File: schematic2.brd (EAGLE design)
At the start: 101.6 x 53.3 mm, 76 parts, among them IC6 DS3231/SO

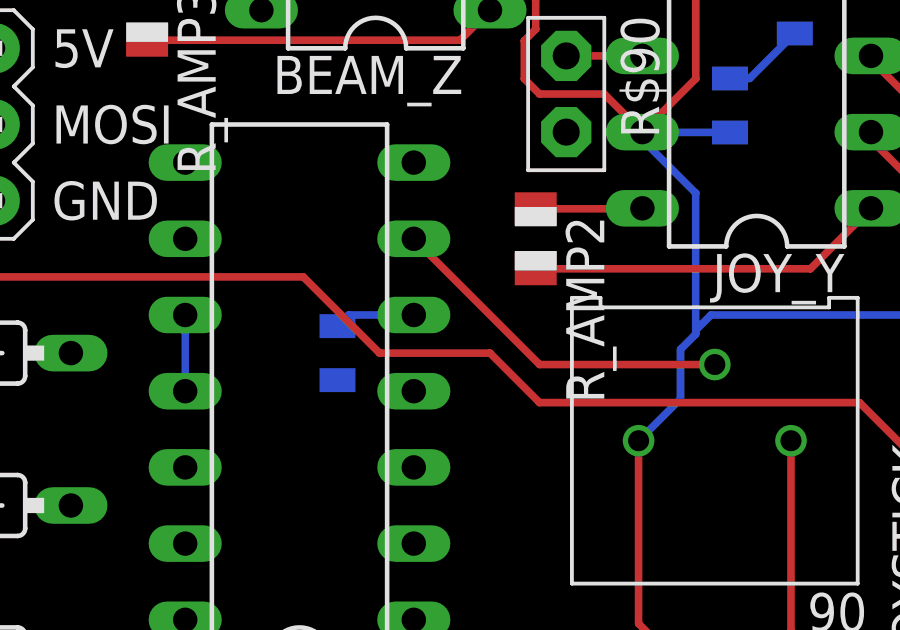
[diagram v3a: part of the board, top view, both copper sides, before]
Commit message: Corrected unity gain buffer amplifiers for reference voltages into the instrumentation amps.
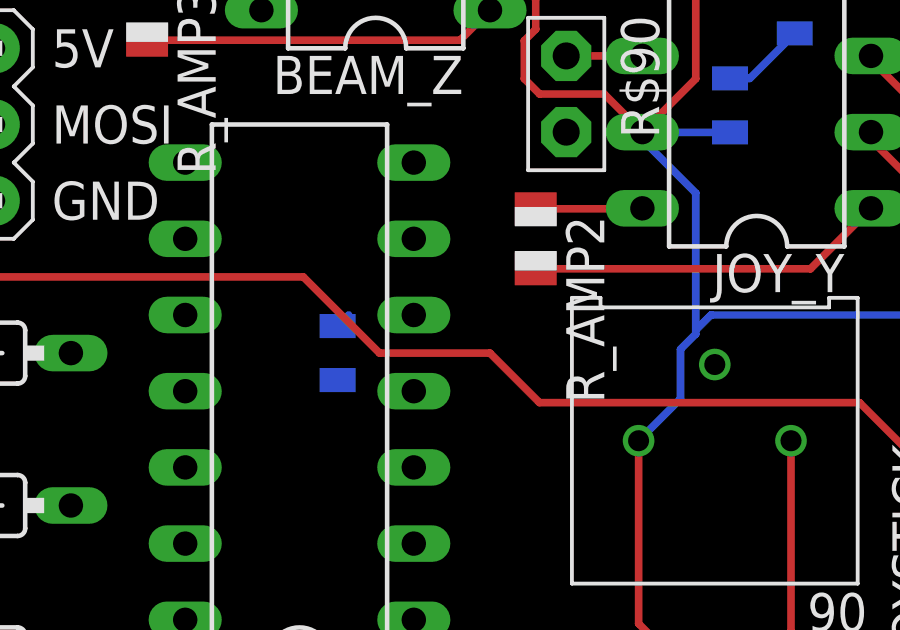
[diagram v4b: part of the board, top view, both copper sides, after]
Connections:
- new net REF_BEAM: BEAM_Z.5, REF.8, REF.9
- new net REF_JOYX: JOY_Y.5, REF.6, REF.7
- new net REF_JOYY: JOY_X.5, REF.1, REF.2
- net A3: now also REF.3; no longer JOY_X.5, REF.1, REF.2
- net A4: now also REF.5; no longer JOY_Y.5, REF.6, REF.7
- net A5: now also REF.10; no longer BEAM_Z.5, REF.8, REF.9
- net AGND: no longer REF.10, REF.3, REF.5
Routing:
- net A4: track 14.3 -> 2.54 mm
- net AGND: track 24.3 -> 19.6 mm
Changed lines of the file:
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@@
 <?xml version="1.0" encoding="utf-8"?>
 <!DOCTYPE eagle SYSTEM "eagle.dtd">
-<eagle version="7.2.0">
+<eagle version="7.0.0">
 <drawing>
 <settings>
@@
 <signals>
 <signal name="A4">
-<contactref element="REF" pad="6"/>
-<contactref element="JOY_Y" pad="5"/>
-<contactref element="REF" pad="7"/>
-<contactref element="90" pad="P$2-WIPER"/>
-<contactref element="4H" pad="A"/>
-<contactref element="4L" pad="C"/>
 <contactref element="U$1" pad="A4"/>
 <contactref element="ANALOG_IN" pad="4"/>
 <wire x1="60.96" y1="2.54" x2="60.96" y2="5.08" width="0.4064" layer="1"/>
-<wire x1="90.043" y1="19.939" x2="84.201" y2="19.939" width="0.254" layer="1"/>
-<wire x1="84.201" y1="19.939" x2="80.01" y2="24.13" width="0.254" layer="1"/>
-<wire x1="80.01" y1="26.67" x2="87.63" y2="32.766" width="0" layer="19" extent="1-1"/>
-<wire x1="80.01" y1="24.13" x2="80.01" y2="26.67" width="0" layer="19" extent="1-1"/>
-<wire x1="64.77" y1="12.7" x2="80.01" y2="24.13" width="0" layer="19" extent="1-1"/>
+<contactref element="4L" pad="C"/>
+<contactref element="90" pad="P$2-WIPER"/>
+<contactref element="4H" pad="A"/>
+<contactref element="REF" pad="5"/>
+<wire x1="80.01" y1="21.59" x2="90.043" y2="19.939" width="0" layer="19" extent="1-1"/>
+<wire x1="64.77" y1="12.7" x2="80.01" y2="21.59" width="0" layer="19" extent="1-1"/>
 <wire x1="60.96" y1="15.24" x2="64.77" y2="12.7" width="0" layer="19" extent="1-1"/>
 <wire x1="60.96" y1="5.08" x2="64.77" y2="12.7" width="0" layer="19" extent="1-1"/>
@@
 </signal>
 <signal name="A3">
-<contactref element="REF" pad="2"/>
-<contactref element="80" pad="P$2-WIPER"/>
-<contactref element="3H" pad="A"/>
-<contactref element="3L" pad="C"/>
-<contactref element="REF" pad="1"/>
-<contactref element="JOY_X" pad="5"/>
 <contactref element="U$1" pad="A3"/>
 <contactref element="ANALOG_IN" pad="5"/>
 <wire x1="58.42" y1="2.54" x2="58.42" y2="5.08" width="0.4064" layer="1"/>
-<wire x1="80.01" y1="13.97" x2="91.44" y2="43.053" width="0" layer="19" extent="1-1"/>
-<wire x1="80.01" y1="11.43" x2="80.01" y2="13.97" width="0" layer="19" extent="1-1"/>
-<wire x1="86.36" y1="9.652" x2="80.01" y2="11.43" width="0" layer="19" extent="1-1"/>
-<wire x1="64.77" y1="7.62" x2="80.01" y2="11.43" width="0" layer="19" extent="1-1"/>
+<contactref element="80" pad="P$2-WIPER"/>
+<contactref element="3L" pad="C"/>
+<contactref element="3H" pad="A"/>
+<contactref element="REF" pad="3"/>
+<wire x1="80.01" y1="16.51" x2="91.44" y2="43.053" width="0" layer="19" extent="1-1"/>
+<wire x1="64.77" y1="7.62" x2="80.01" y2="16.51" width="0" layer="19" extent="1-1"/>
 <wire x1="60.96" y1="10.16" x2="64.77" y2="7.62" width="0" layer="19" extent="1-1"/>
 <wire x1="58.42" y1="5.08" x2="60.96" y2="10.16" width="0" layer="19" extent="1-1"/>
@@
 </signal>
 <signal name="A5">
-<contactref element="BEAM_Z" pad="5"/>
-<contactref element="REF" pad="8"/>
-<contactref element="REF" pad="9"/>
-<contactref element="70" pad="P$2-WIPER"/>
-<contactref element="5H" pad="A"/>
-<contactref element="5L" pad="C"/>
 <contactref element="U$1" pad="A5"/>
 <contactref element="ANALOG_IN" pad="3"/>
 <wire x1="63.5" y1="2.54" x2="63.5" y2="5.08" width="0.4064" layer="1"/>
-<wire x1="74.93" y1="39.37" x2="71.12" y2="49.53" width="0" layer="19" extent="1-1"/>
-<wire x1="72.39" y1="26.67" x2="74.93" y2="39.37" width="0" layer="19" extent="1-1"/>
-<wire x1="72.39" y1="24.13" x2="72.39" y2="26.67" width="0" layer="19" extent="1-1"/>
-<wire x1="64.77" y1="17.78" x2="72.39" y2="24.13" width="0" layer="19" extent="1-1"/>
+<contactref element="5H" pad="A"/>
+<contactref element="70" pad="P$2-WIPER"/>
+<contactref element="5L" pad="C"/>
+<contactref element="REF" pad="10"/>
+<wire x1="72.39" y1="21.59" x2="71.12" y2="49.53" width="0" layer="19" extent="1-1"/>
+<wire x1="64.77" y1="17.78" x2="72.39" y2="21.59" width="0" layer="19" extent="1-1"/>
 <wire x1="60.96" y1="20.32" x2="64.77" y2="17.78" width="0" layer="19" extent="1-1"/>
 <wire x1="63.5" y1="5.08" x2="64.77" y2="17.78" width="0" layer="19" extent="1-1"/>
@@
 <contactref element="4L" pad="A"/>
 <contactref element="1L" pad="A"/>
-<contactref element="REF" pad="5"/>
 <contactref element="AMP" pad="5"/>
 <contactref element="C90" pad="1"/>
@@
 <contactref element="AMP" pad="10"/>
 <contactref element="2L" pad="A"/>
-<contactref element="REF" pad="10"/>
 <contactref element="5L" pad="A"/>
 <contactref element="SJ1" pad="1"/>
 <contactref element="TMP102" pad="3"/>
-<contactref element="REF" pad="3"/>
 <contactref element="AMP" pad="3"/>
 <contactref element="C91" pad="2"/>
@@
 <wire x1="52.97" y1="31.623" x2="52.97" y2="29.58" width="0.254" layer="16"/>
 <wire x1="52.97" y1="29.58" x2="53.34" y2="29.21" width="0.254" layer="16"/>
-<wire x1="80.01" y1="21.59" x2="77.84" y2="21.59" width="0.254" layer="16"/>
 <wire x1="77.84" y1="21.59" x2="77.47" y2="21.22" width="0.254" layer="16"/>
-<wire x1="72.39" y1="19.05" x2="72.39" y2="21.59" width="0.254" layer="16"/>
 <wire x1="50.8" y1="36.83" x2="53.34" y2="36.83" width="0.254" layer="16"/>
 <wire x1="52.97" y1="31.623" x2="52.97" y2="36.46" width="0.254" layer="16"/>
 <wire x1="52.97" y1="36.46" x2="53.34" y2="36.83" width="0.254" layer="16"/>
-<wire x1="80.01" y1="21.59" x2="90.551" y2="29.475" width="0" layer="19" extent="16-16"/>
-<wire x1="80.01" y1="16.51" x2="80.01" y2="21.59" width="0" layer="19" extent="1-1"/>
-<wire x1="72.39" y1="21.59" x2="77.47" y2="21.22" width="0" layer="19" extent="16-16"/>
-<wire x1="68.58" y1="20.32" x2="72.39" y2="21.59" width="0" layer="19" extent="1-1"/>
+<wire x1="80.01" y1="37.581" x2="90.551" y2="29.475" width="0" layer="19" extent="16-16"/>
+<wire x1="77.84" y1="21.59" x2="77.47" y2="36.206" width="0" layer="19" extent="16-16"/>
+<wire x1="72.39" y1="19.05" x2="77.47" y2="21.22" width="0" layer="19" extent="16-16"/>
+<wire x1="68.58" y1="20.32" x2="72.39" y2="19.05" width="0" layer="19" extent="1-1"/>
 <wire x1="68.58" y1="15.24" x2="68.58" y2="20.32" width="0" layer="19" extent="1-1"/>
 <wire x1="68.58" y1="10.16" x2="68.58" y2="15.24" width="0" layer="19" extent="1-1"/>
 <wire x1="73.49" y1="6.35" x2="68.58" y2="10.16" width="0" layer="19" extent="1-1"/>
 <wire x1="76.2" y1="2.54" x2="73.49" y2="6.35" width="0" layer="19" extent="1-1"/>
-<wire x1="80.01" y1="37.581" x2="90.551" y2="29.475" width="0" layer="19" extent="16-16"/>
 <wire x1="89.408" y1="6.361" x2="76.2" y2="2.54" width="0" layer="19" extent="16-16"/>
 <wire x1="53.34" y1="20.32" x2="68.58" y2="20.32" width="0" layer="19" extent="1-1"/>
@@
 <wire x1="87.63" y1="30.226" x2="85.09" y2="30.226" width="0.254" layer="1"/>
 </signal>
+<signal name="REF_BEAM">
+<contactref element="BEAM_Z" pad="5"/>
+<contactref element="REF" pad="9"/>
+<contactref element="REF" pad="8"/>
+<wire x1="72.39" y1="26.67" x2="74.93" y2="39.37" width="0" layer="19" extent="1-1"/>
+<wire x1="72.39" y1="24.13" x2="72.39" y2="26.67" width="0" layer="19" extent="1-1"/>
+</signal>
+<signal name="REF_JOYX">
+<contactref element="REF" pad="6"/>
+<contactref element="REF" pad="7"/>
+<contactref element="JOY_Y" pad="5"/>
+<wire x1="80.01" y1="26.67" x2="87.63" y2="32.766" width="0" layer="19" extent="1-1"/>
+<wire x1="80.01" y1="24.13" x2="80.01" y2="26.67" width="0" layer="19" extent="1-1"/>
+</signal>
+<signal name="REF_JOYY">
+<contactref element="REF" pad="2"/>
+<contactref element="REF" pad="1"/>
+<contactref element="JOY_X" pad="5"/>
+<wire x1="80.01" y1="11.43" x2="86.36" y2="9.652" width="0" layer="19" extent="1-1"/>
+<wire x1="80.01" y1="13.97" x2="80.01" y2="11.43" width="0" layer="19" extent="1-1"/>
+</signal>
 </signals>

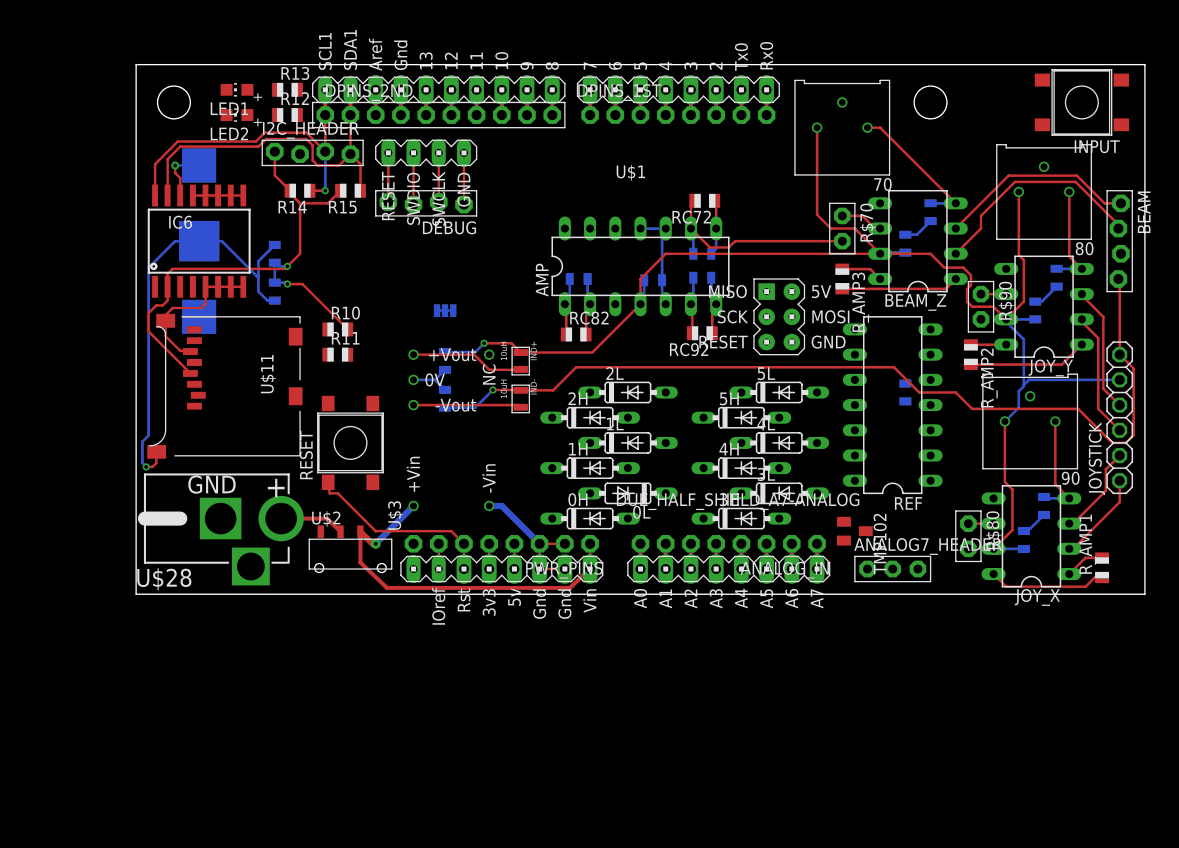
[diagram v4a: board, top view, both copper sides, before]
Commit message: Moved the amps around again, wired most of the traces. Discovered that I never connected CS_SD, it is now wired to Due pin D10.
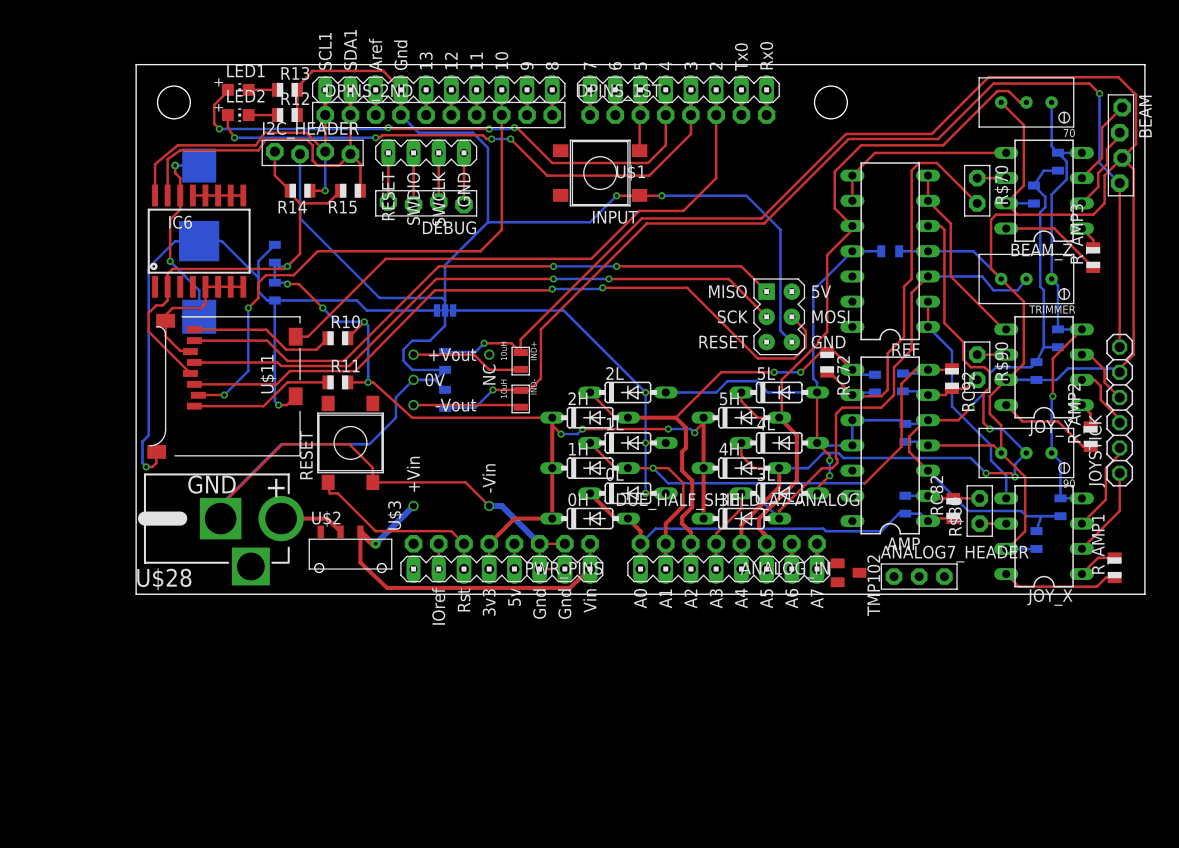
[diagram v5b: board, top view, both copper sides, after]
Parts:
- removed 80: TRIM-POT, Felicia_force_logger:R-TRIMMER-BOURNS-3386P
- added TRIMMER: 100k ohm, Felicia_force_logger:R-TRIMMER_67W_TT_ELEC
- 3H: value DIODE_ZENERDO-35_AXIAL -> 3.6V_DIODE
- 70, 90: value TRIM-POT -> 100k ohm; device Felicia_force_logger:R-TRIMMER-BOURNS-3386P -> miller:R-TRIMMER_67W_TT_ELEC
- moved INPUT 49.0 mm to (46.7, 42.4)
- moved RC82 41.8 mm to (82.3, 8.64), turned to 90 degrees
- moved C82 40.0 mm to (77.5, 9.02), turned to 90 degrees
- moved AMP 30.9 mm to (75.9, 15.0), turned to 90 degrees
- moved C17 29.7 mm to (77.5, 16.3), turned to 270 degrees
- moved RC92 25.6 mm to (82.2, 21.7), turned to 270 degrees
- moved R_AMP3 25.4 mm to (96.4, 33.9), turned to 90 degrees
- moved C92 22.8 mm to (77.2, 21.3), turned to 270 degrees
- moved C72 21.8 mm to (74.4, 21.2), turned to 270 degrees
- moved RC72 20.4 mm to (69.6, 23.4), turned to 270 degrees
- moved 70 18.7 mm to (89.7, 49.5)
- moved REF 15.5 mm to (75.9, 34.5)
- moved R_AMP2 14.6 mm to (96.1, 15.9), turned to 90 degrees
- moved C16 14.3 mm to (75.9, 34.5), turned to 180 degrees
- moved R$70 14.1 mm to (84.7, 40.6)
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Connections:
- removed net D10: DPINS_2ND.8, U$1.10
- net +5V: now also TRIMMER.P$3; no longer 80.P$3
- net A3: now also TRIMMER.P$2; no longer 80.P$2-WIPER
- net A4: now also 90.P$2; no longer 90.P$2-WIPER
- net A5: now also 70.P$2; no longer 70.P$2-WIPER
- net CS_SD: now also DPINS_2ND.8, U$1.10
- net VNEG: now also TRIMMER.P$1; no longer 80.P$1
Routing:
- net GND: track 21.8 -> 207.2 mm, vias 0 -> 2
- net AGND: track 19.6 -> 160.8 mm, vias 0 -> 6
- net +3V3: track 58.3 -> 135.2 mm, vias 2 -> 9
- net +5V: track 145.0 -> 221.6 mm
- net A4: track 2.54 -> 75.4 mm, vias 0 -> 3
- net MOSI: track 0.00 -> 72.7 mm, vias 0 -> 2
- net A5: track 2.54 -> 74.9 mm
- net MISO: track 0.00 -> 63.5 mm, vias 0 -> 2
- net SCLK: track 0.00 -> 63.0 mm, vias 0 -> 2
- net CS_SD: track 0.00 -> 56.2 mm, vias 0 -> 2
- net A3: track 2.54 -> 58.3 mm
- net CARD_DETECT: track 2.54 -> 57.9 mm
- net LED_GREEN: track 2.54 -> 57.6 mm, vias 0 -> 4
- net LED_RED: track 2.54 -> 56.4 mm, vias 0 -> 4
- net A1: track 8.50 -> 62.4 mm, vias 0 -> 1
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
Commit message: Swapped out I2C header with a 6 pin version that could work with Adafruit I2C OLED display. Moved Reset button to upper corner like the Due's location. Moved LEDs closer to their associated digital pins. Finished wiring the analog and digital sections. Need to deal with ground planes on bottom still.
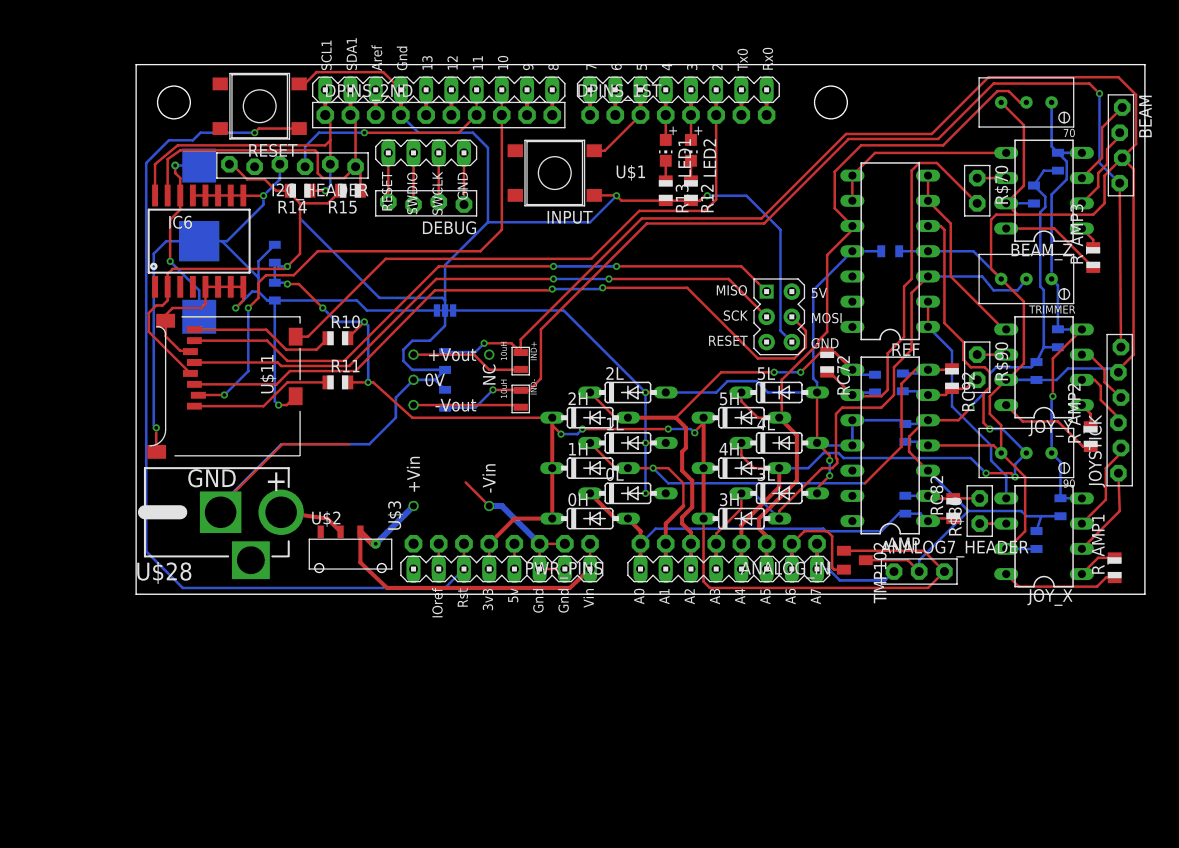
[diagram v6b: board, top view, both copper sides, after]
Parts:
- ANALOG7_HEADER: value PINHD-1X3 -> (none)
- BEAM: device Felicia_force_logger:1X04_BIGLOCK -> Felicia_force_logger:1X04_LOCK
- DEBUG: value PINHD-1X4 -> (none); device Felicia_force_logger:1X04_BIGLOCK -> Felicia_force_logger:1X04_LOCK
- I2C_HEADER: value PINHD-1X4 -> (none); device Felicia_force_logger:1X04_BIGLOCK -> Felicia_force_logger:1X06-LOCK
- JOYSTICK: device Felicia_force_logger:1X06 -> Felicia_force_logger:1X06-LOCK
- R$70, R$80, R$90: value PINHD-1X2 -> (none)
- moved LED2 45.7 mm to (55.9, 44.7), turned to 180 degrees
- moved LED1 43.5 mm to (53.3, 44.7), turned to 180 degrees
- moved R12 41.3 mm to (55.9, 40.6), turned to 270 degrees
- moved R13 39.4 mm to (53.3, 40.6), turned to 270 degrees
- moved RESET 35.1 mm to (12.4, 49.1), turned to 180 degrees
- moved INPUT 4.57 mm to (42.2, 42.4)
- moved I2C_HEADER 2.40 mm to (15.7, 43.2), turned to 180 degrees
- moved TMP102 1.42 mm to (72.4, 3.43)
- moved U$28 0.64 mm to (14.6, 8.26)
- moved ANALOG7_HEADER 0.51 mm to (78.9, 2.29)
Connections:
- removed net D11: DPINS_2ND.7, U$1.11
- removed net NC: PWR_PINS.8
- new net I2C_RES: DPINS_2ND.7, I2C_HEADER.3, U$1.11
- net +3V3: now also I2C_HEADER.6; no longer I2C_HEADER.1
- net DGND: now also I2C_HEADER.4
- net GND: no longer I2C_HEADER.2
- net SCL1: now also I2C_HEADER.2; no longer I2C_HEADER.3
- net SDA1: now also I2C_HEADER.1; no longer I2C_HEADER.4
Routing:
- net RESET: track 19.3 -> 92.8 mm, vias 0 -> 1
- net LED_GREEN: track 57.6 -> 5.05 mm, vias 4 -> 0
- net LED_RED: track 56.4 -> 5.05 mm, vias 4 -> 0
- net +3V3: track 135.2 -> 180.4 mm
- net I2C_RES: track 0.00 -> 23.2 mm, vias 0 -> 1
- net GND: track 207.2 -> 184.6 mm
- net DGND: track 93.8 -> 107.9 mm, vias 2 -> 4
- net AGND: track 160.8 -> 174.8 mm
- net A6: track 2.54 -> 11.8 mm
- net A7: track 2.54 -> 11.1 mm
- net BUTTON1: track 6.17 -> 8.81 mm
- net D11: track 2.54 -> 0.00 mm
- net CARD_DETECT: track 57.9 -> 59.1 mm
- net N$37: track 2.90 -> 2.01 mm
- net N$36: track 2.90 -> 2.01 mm
